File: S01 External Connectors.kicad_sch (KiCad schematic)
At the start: 43 parts, among them J1 1053101204, J2 1053101114, J3 10144517-043802LF, J4 1053102204, J5 1053091102, J6 1053091102, M1 78614150960, M2 78614150960, M3 78614150960, M4 78614150960, M5 78614150960, M6 78614150960

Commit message: Drop the BON name from the test points
TP1-TP26 are test points. The Altium "BON" (bed of nails) name added
nothing the TP designator and POGO-1 value don't already say.

- Footprint TEST PIN BON 1-25mm SMD Pad (POGO-1) -> TEST PIN 1-25mm
  SMD Pad (POGO-1); symbol Test Pin BON ... -> Test Pin ...; all
  references on S01 and the PCB, and the footprint filters, follow.
- README and the .kicad_dru comment call them test points.

Co-Authored-By: Claude Opus 5.5 <noreply@anthropic.com>
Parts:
- TP1, TP10, TP11, TP12, TP13, TP14, TP15, TP16, TP17, TP18, TP19, TP2, TP20, TP21, TP22, TP23, TP24, TP25, TP26, TP3, TP4, TP5, TP6, TP7, TP8, TP9: footprint EVO2513-0_5_0-import-fps:TEST PIN BON 1-25mm SMD Pad (POGO-1) -> EVO2513-0_5_0-import-fps:TEST PIN 1-25mm SMD Pad (POGO-1); symbol Lattech Systems:Test Pin BON 1-25mm SMD Pad (POGO-1) -> Lattech Systems:Test Pin 1-25mm SMD Pad (POGO-1)

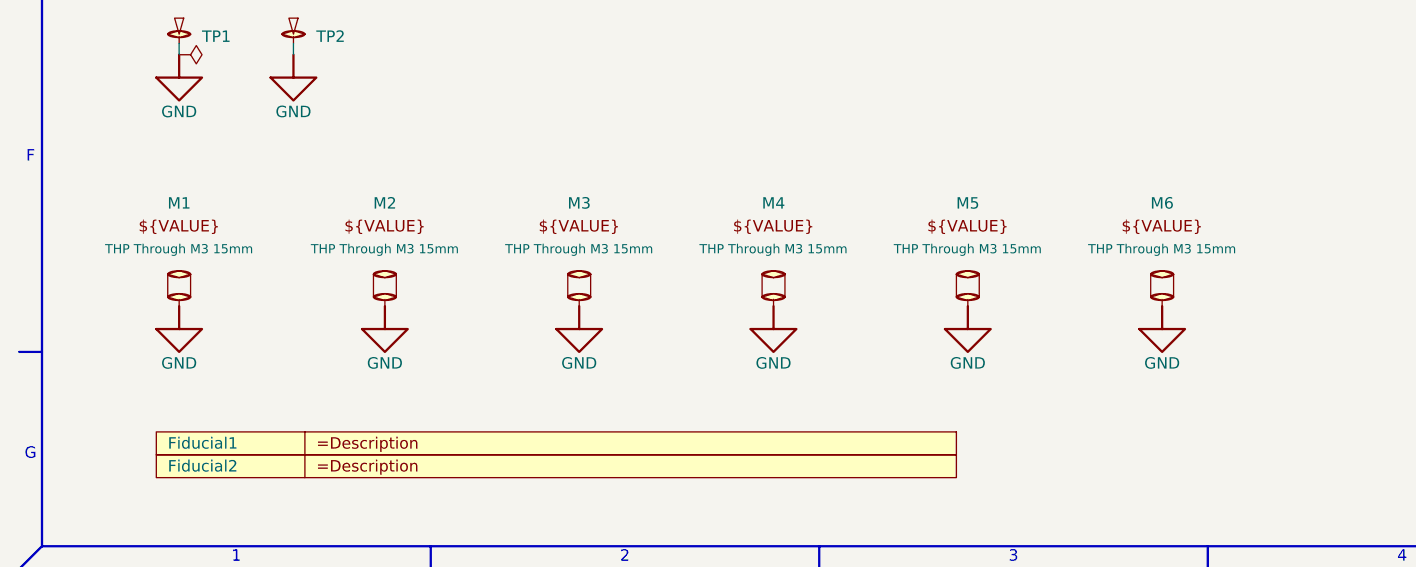
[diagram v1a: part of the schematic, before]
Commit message: Spacer thermal reliefs on the pad instead of keepout arcs
M1-M6: pad thermal relief, 2 mm spokes at 90 deg, 0.4 mm gap, set in the
library footprint as well as on the board. The four keepout arcs are
removed from the footprint. A DRC rule keeps other-net pours 0.45 mm from
M6, between the DCCHARGER and DCPATH pours.

Co-Authored-By: Claude Opus 5.5 <noreply@anthropic.com>
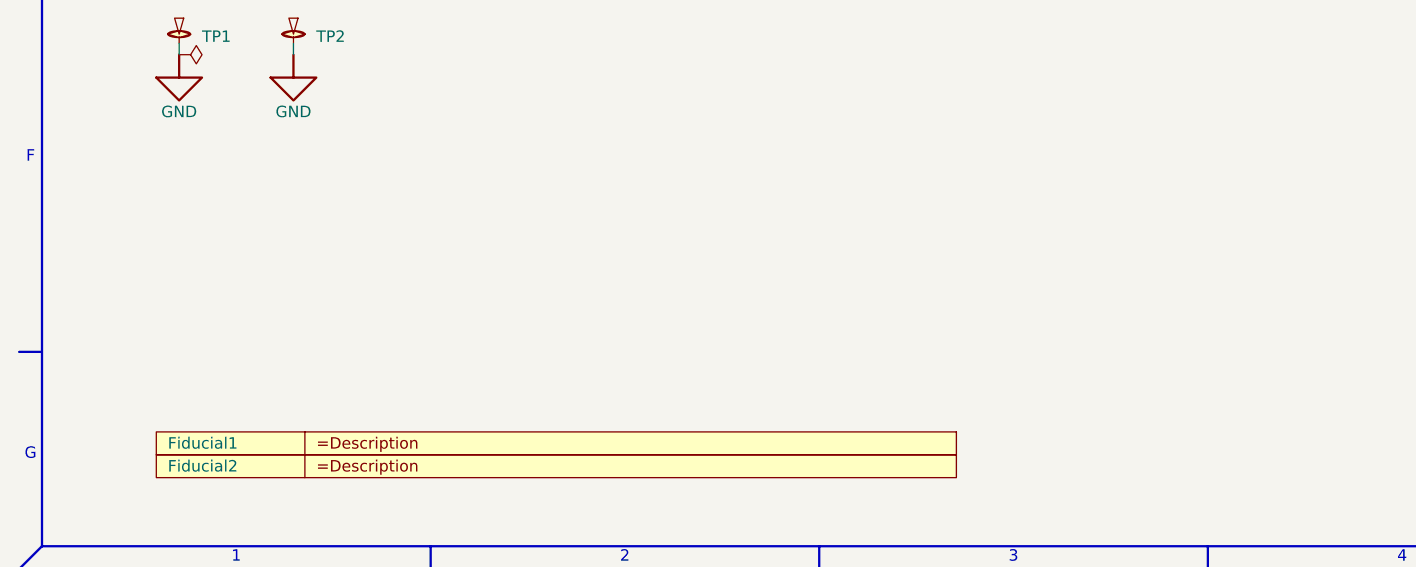
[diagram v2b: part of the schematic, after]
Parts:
- removed M1, M2, M3, M4, M5, M6: 78614150960, EVO2513-0_5_0-import-fps:MECH SPACER WURTH 78614150960 THROUGH M3, symbol Lattech Systems:Mech Spacer Wurth 78614150960 Through M3 15mm

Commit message: Raise divider impedances, dim the PG LEDs, use standard diode lands
TI asks for a pull-up of at least 350 kOhm on EN/UVLO above 5 V.
R108 100K -> 619K and R49 12K -> 75K, both values already on the
BOM: turn-on 11.10 V (10.63-11.91 V worst case), off 10.09 V. 1M/120K
was rejected because leakage across 1M puts worst-case turn-on at
12.24 V, above the rail.

Q24 gate bias R109 100K -> 1.07M and R110 27K -> 390K: +12V draw
94 -> 8.2 uA, gate 3.2 V at 12 V and under 4 V worst case at the
14.7 V OVLO limit. The R115 bypass pull-down is now 62.9K.

PGTH dividers R59/R61/R76 100K -> 390K and R60/R62/R77 13K -> 51K:
PG at 10.38 V (11.17 V worst case), 23.5 uA at threshold to meet TI's
20x PGTH leakage rule. 390K is the only new BOM value.

PG LED resistors R67/R68/R81 2.2K -> 4.7K, about 0.9 mA less on
battery with all rails up.

D1, D4, D6-D10 and LED1-LED4 move from imported Altium lands to KiCad
standard footprints (D_SMB, D_SMA, SOT-23, Diodes_UDFN-10, LED_0603),
in place with the same nets; the LEDs turn 180 deg for pad 1. Drops
the 8 thin LED A/C silk warnings. Five unused imported footprints
removed. Nearby parts and tracks adjusted for the new lands.

Keep the GND planes free of power copper, as on the original: remove
the SW1/L2 and SW2 strip zones and the small +12V (via block by R115)
and U5 ISNSP (under Q18's drain) zones from In1/In3/In5/In6. They
carried no current; GND gains about 0.8 mm2 on In1, 3.5 mm2 on In3
and In5 and 3.7 mm2 on In6 under the power stage.

Remove the 347 via-block octagons the Altium import left as copper
graphic polygons (gr_poly) on B.Cu and In1-In6, one 1.2 x 1.8 mm
octagon per six-via block per layer. As drawings they bypassed zone
rules, and on the GND layers they were net islands in the pour,
including the charger switch node. None carried current: same-net
pours connect the vias solid, and DRC finds 0 unconnected. GND gains
about 26 mm2 on In1, 21 mm2 on In3 and In5, 18 mm2 on In6 and 27 mm2
on B.Cu.

Rename TPS22811 pin 2 to nEN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
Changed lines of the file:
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@@
-	)
-	(symbol
-		(lib_id "power:PWR_FLAG")
-		(at 160.02 102.87 270)
-		(unit 1)
-		(body_style 1)
-		(exclude_from_sim no)
-		(in_bom yes)
-		(on_board yes)
-		(in_pos_files yes)
-		(dnp no)
-		(property "Reference" "#FLG02"
-			(at 161.925 102.87 0)
-			(hide yes)
-			(show_name no)
-			(do_not_autoplace no)
-			(effects
-				(font
-					(size 1.27 1.27)
-				)
-			)
-		)
-		(property "Value" "PWR_FLAG"
-			(at 163.83 102.87 0)
-			(hide yes)
-			(show_name no)
-			(do_not_autoplace no)
-			(effects
-				(font
-					(size 1.27 1.27)
-				)
-			)
-		)
-		(property "Footprint" ""
-			(at 160.02 102.87 0)
-			(hide yes)
-			(show_name no)
-			(do_not_autoplace no)
-			(effects
-				(font
-					(size 1.27 1.27)
-				)
-			)
-		)
-		(property "Datasheet" "~"
-			(at 160.02 102.87 0)
-			(hide yes)
-			(show_name no)
-			(do_not_autoplace no)
-			(effects
-				(font
-					(size 1.27 1.27)
-				)
-			)
-		)
-		(property "Description" "Special symbol for telling ERC where power comes from"
-			(at 160.02 102.87 0)
-			(hide yes)
-			(show_name no)
-			(do_not_autoplace no)
-			(effects
-				(font
-					(size 1.27 1.27)
-				)
-			)
-		)
-		(pin "1"
-		)
-		(instances
-			(project "EVO2513"
-				(path "/44203427-0a3b-455b-9bb9-c1b577d179b3/49489d81-6ed3-4223-b712-58477545f8f8"
-					(reference "#FLG02")
-					(unit 1)
-				)
-			)
-		)
 	)
 	(symbol

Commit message: Fill manufacturer part numbers from the 0.5.0 build orders
Set MANUFACTURER and MANUFACTURER_PN on every fitted part, in the
schematic and on the board. Unchanged parts take the exact part numbers
ordered for the 0.5.0 backup build (DigiKey list and Mouser basket);
changed parts reuse an ordered part where value, package and rating
match; the rest keep the schematic's part or take a Yageo RC/CC part.

Co-Authored-By: Claude Opus 5.5 <noreply@anthropic.com>
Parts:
- J3: MANUFACTURER Amphenol -> Amphenol ICC (FCI)
- R28: MANUFACTURER ? -> YAGEO; MANUFACTURER_PN ? -> RC0402FR-0710KL
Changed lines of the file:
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@@
 			)
 		)
-		(property "MANUFACTURER" "Amphenol"
+		(property "MANUFACTURER" "Amphenol ICC (FCI)"
 			(at 184.912 93.98 0)
 			(hide yes)
@@
 			)
 		)
-		(property "MANUFACTURER" "?"
+		(property "MANUFACTURER" "YAGEO"
 			(at 230.124 168.402 0)
 			(hide yes)
@@
 			)
 		)
-		(property "MANUFACTURER_PN" "?"
+		(property "MANUFACTURER_PN" "RC0402FR-0710KL"
 			(at 230.124 168.402 0)
 			(hide yes)
